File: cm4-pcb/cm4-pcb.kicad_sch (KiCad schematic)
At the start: 35 parts, among them J1 Conn_01x02_Pin, J2 Conn_01x02_Pin, J3 USB1125-GF-B, J4 Conn_02x03_Odd_Even, J5 Conn_01x04, J6 J0011D21NL, J7 Conn_01x02, J8 Conn_01x02, U1 Pfostenstecker_6_2x3, U2 Pfostenstecker_6_2x3, U5 SMD-PUSH-BTN

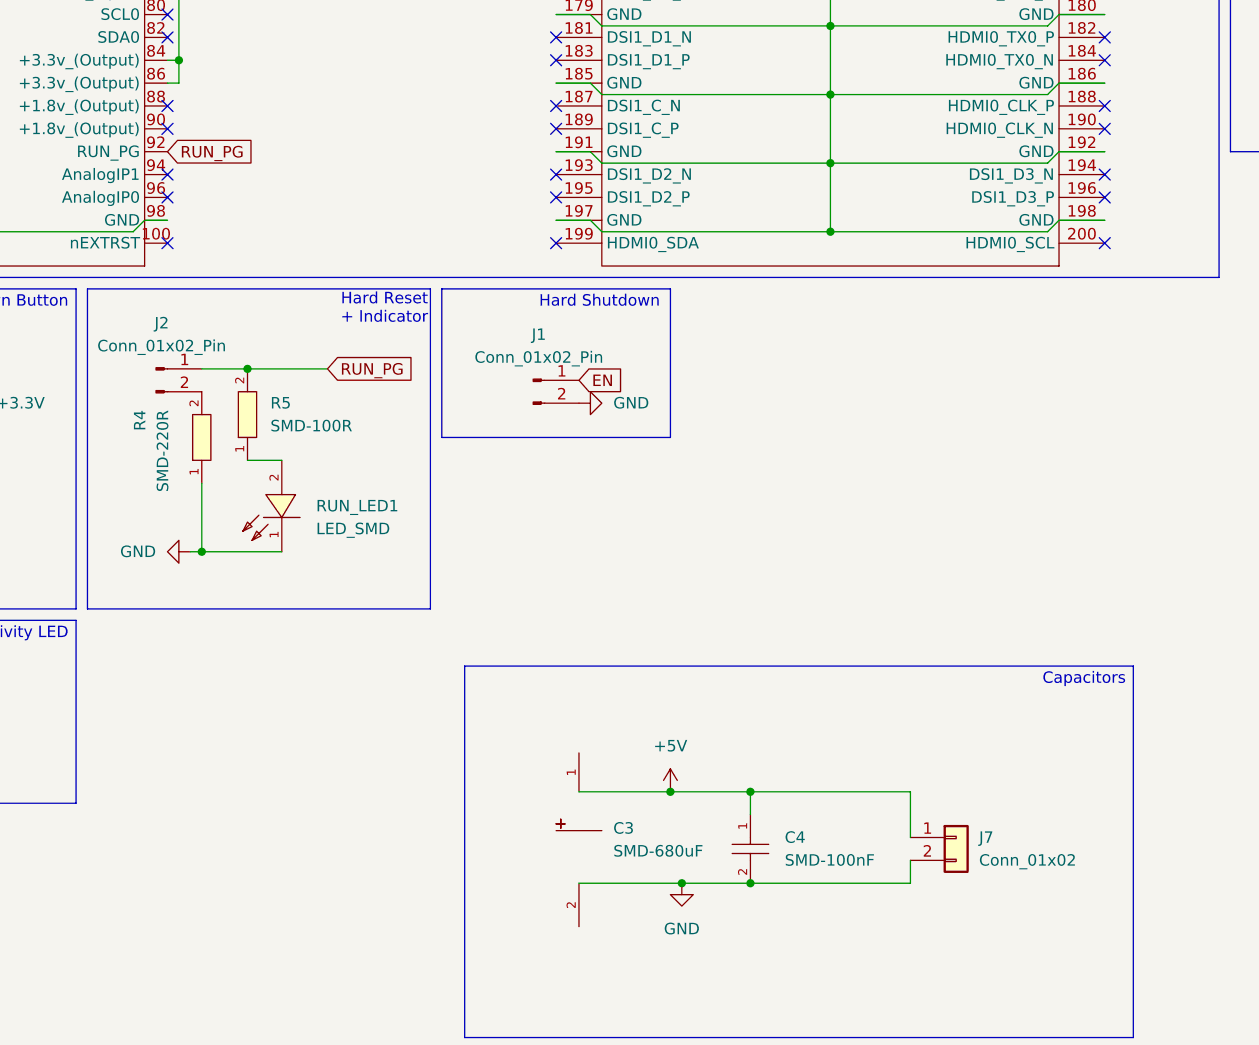
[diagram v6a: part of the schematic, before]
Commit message: Pins Analog Input
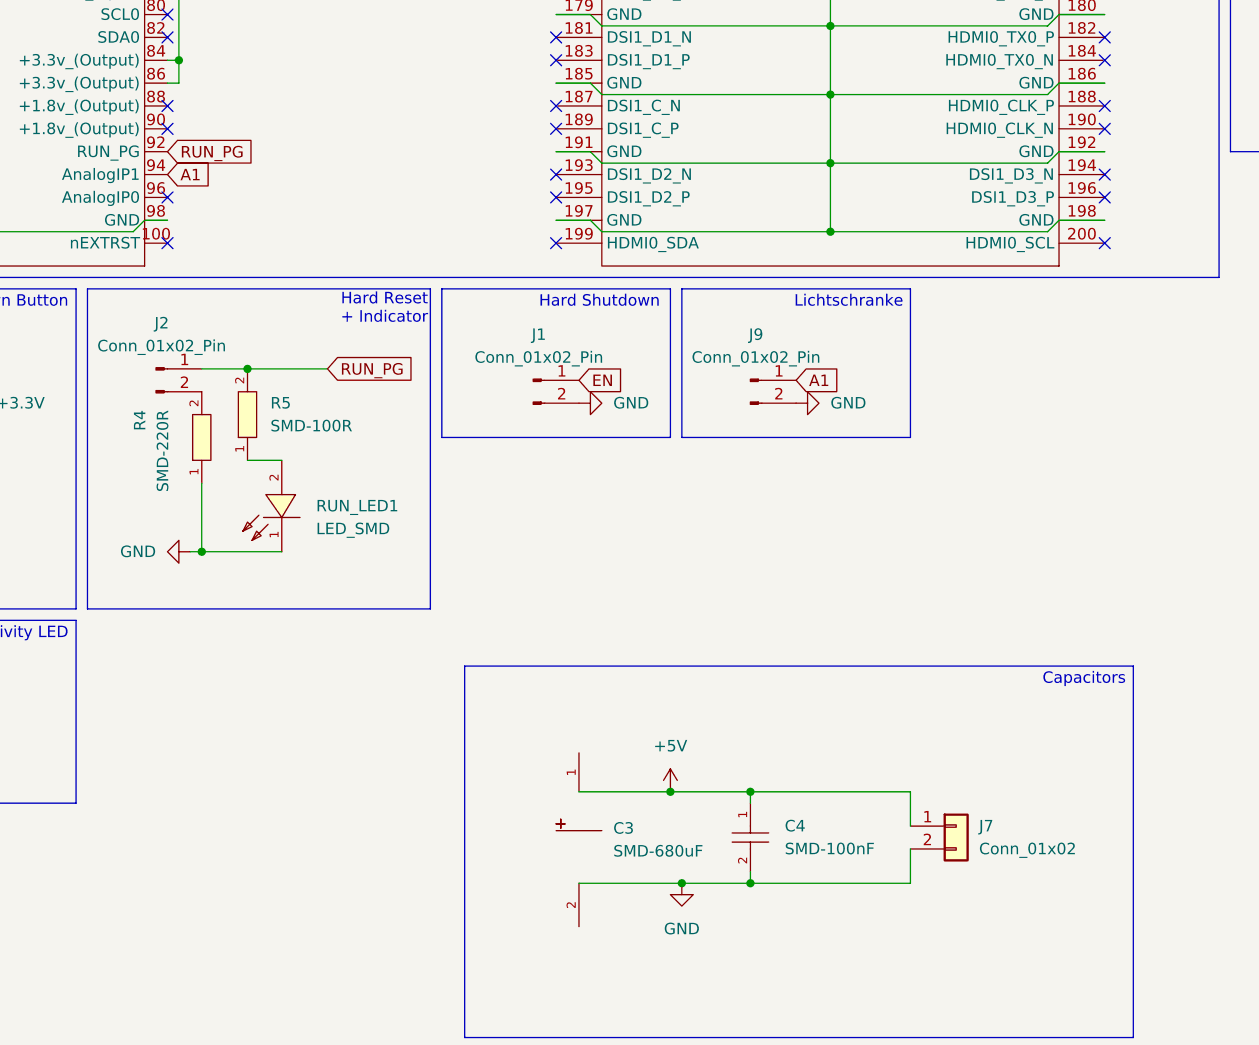
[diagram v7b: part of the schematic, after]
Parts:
- added J9: Conn_01x02_Pin, Connector_PinHeader_2.54mm:PinHeader_1x02_P2.54mm_Vertical, symbol Connector:Conn_01x02_Pin
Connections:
- net GND: now also J9.2 (Pin_2)
- net A1: now reaches Module1.94 (AnalogIP1)
- net A1: now also J9.1 (Pin_1)
- no-connect marks 126 -> 125
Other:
- note added: "Lichtschranke"
- moved on the sheet: C4, J7
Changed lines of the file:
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@@
 	)
 	(no_connect
-		(at 86.36 144.78)
-	)
-	(no_connect
 		(at 86.36 127)
 	)
@@
 	(wire
 		(pts
-			(xy 168.91 213.36) (xy 168.91 218.44)
+			(xy 168.91 213.36) (xy 168.91 217.17)
 		)
 		(stroke
@@
 	(wire
 		(pts
-			(xy 151.13 213.36) (xy 151.13 215.9)
+			(xy 151.13 213.36) (xy 151.13 214.63)
 		)
 		(stroke
@@
 	(wire
 		(pts
+			(xy 151.13 222.25) (xy 151.13 223.52)
+		)
+		(stroke
+			(width 0)
+			(type default)
+		)
+	)
+	(wire
+		(pts
 			(xy 55.88 95.25) (xy 55.88 102.87)
 		)
@@
 	(wire
 		(pts
-			(xy 168.91 220.98) (xy 168.91 223.52)
+			(xy 168.91 219.71) (xy 168.91 223.52)
 		)
 		(stroke
@@
 		)
 	)
+	(rectangle
+		(start 143.51 157.48)
+		(end 168.91 173.99)
+		(stroke
+			(width 0)
+			(type default)
+		)
+		(fill
+			(type none)
+		)
+	)
 	(text "Ethernet Magjack"
 		(exclude_from_sim no)
@@
 		)
 	)
+	(text "Lichtschranke"
+		(exclude_from_sim no)
+		(at 162.052 159.004 0)
+		(effects
+			(font
+				(size 1.27 1.27)
+			)
+		)
+	)
 	(text "Grounded for fixed use as USB Host, datasheet chapter 2.4 and pinout"
 		(exclude_from_sim no)
@@
 		)
 	)
+	(global_label "A1"
+		(shape input)
+		(at 156.21 167.64 0)
+		(fields_autoplaced yes)
+		(effects
+			(font
+				(size 1.27 1.27)
+			)
+			(justify left)
+		)
+		(property "Intersheetrefs" "${INTERSHEET_REFS}"
+			(at 161.4933 167.64 0)
+			(effects
+				(font
+					(size 1.27 1.27)
+				)
+				(justify left)
+				(hide yes)
+			)
+		)
+	)
 	(global_label "SDA"
 		(shape bidirectional)
@@
 		)
 	)
+	(global_label "A1"
+		(shape input)
+		(at 86.36 144.78 0)
+		(fields_autoplaced yes)
+		(effects
+			(font
+				(size 1.27 1.27)
+			)
+			(justify left)
+		)
+		(property "Intersheetrefs" "${INTERSHEET_REFS}"
+			(at 91.6433 144.78 0)
+			(effects
+				(font
+					(size 1.27 1.27)
+				)
+				(justify left)
+				(hide yes)
+			)
+		)
+	)
 	(global_label "SDA"
 		(shape bidirectional)
@@
 	)
 	(symbol
+		(lib_id "Connector:Conn_01x02_Pin")
+		(at 151.13 167.64 0)
+		(unit 1)
+		(exclude_from_sim no)
+		(in_bom yes)
+		(on_board yes)
+		(dnp no)
+		(fields_autoplaced yes)
+		(property "Reference" "J9"
+			(at 151.765 162.56 0)
+			(effects
+				(font
+					(size 1.27 1.27)
+				)
+			)
+		)
+		(property "Value" "Conn_01x02_Pin"
+			(at 151.765 165.1 0)
+			(effects
+				(font
+					(size 1.27 1.27)
+				)
+			)
+		)
+		(property "Footprint" "Connector_PinHeader_2.54mm:PinHeader_1x02_P2.54mm_Vertical"
+			(at 151.13 167.64 0)
+			(effects
+				(font
+					(size 1.27 1.27)
+				)
+				(hide yes)
+			)
+		)
+		(property "Datasheet" "~"
+			(at 151.13 167.64 0)
+			(effects
+				(font
+					(size 1.27 1.27)
+				)
+				(hide yes)
+			)
+		)
+		(property "Description" "Generic connector, single row, 01x02, script generated"
+			(at 151.13 167.64 0)
+			(effects
+				(font
+					(size 1.27 1.27)
+				)
+				(hide yes)
+			)
+		)
+		(pin "2"
+		)
+		(pin "1"
+		)
+		(instances
+			(project "cm4-pcb"
+				(path "/498e70b5-f2fd-4a95-9aba-8c3678ffa14c"
+					(reference "J9")
+					(unit 1)
+				)
+			)
+		)
+	)
+	(symbol
 		(lib_id "bohlebots.lib:+5V")
 		(at 364.49 40.64 90)
@@
 	(symbol
 		(lib_id "bohlebots.lib:SMD-100nF")
-		(at 151.13 219.71 270)
+		(at 151.13 218.44 270)
 		(unit 1)
 		(exclude_from_sim no)
@@
 		(fields_autoplaced yes)
 		(property "Reference" "C4"
-			(at 154.94 218.4399 90)
+			(at 154.94 217.1699 90)
 			(effects
 				(font
@@
 		)
 		(property "Value" "SMD-100nF"
-			(at 154.94 220.9799 90)
+			(at 154.94 219.7099 90)
 			(effects
 				(font
@@
 		)
 		(property "Footprint" "BohleBots:C0603"
-			(at 140.97 219.71 0)
+			(at 140.97 218.44 0)
 			(effects
 				(font
@@
 		)
 		(property "Datasheet" "https://item.szlcsc.com/362304.html"
-			(at 153.67 215.9 0)
+			(at 153.67 214.63 0)
 			(effects
 				(font
@@
 		)
 		(property "Description" ""
-			(at 151.13 219.71 0)
+			(at 151.13 218.44 0)
 			(effects
 				(font
@@
 		)
 		(property "LCSC" "C30926"
-			(at 151.13 219.71 0)
+			(at 151.13 218.44 0)
 			(effects
 				(font
@@
 	(symbol
 		(lib_id "Connector_Generic:Conn_01x02")
-		(at 173.99 218.44 0)
+		(at 173.99 217.17 0)
 		(unit 1)
 		(exclude_from_sim no)
@@
 		(fields_autoplaced yes)
 		(property "Reference" "J7"
-			(at 176.53 218.4399 0)
+			(at 176.53 217.1699 0)
 			(effects
 				(font
@@
 		)
 		(property "Value" "Conn_01x02"
-			(at 176.53 220.9799 0)
+			(at 176.53 219.7099 0)
 			(effects
 				(font
@@
 		)
 		(property "Footprint" "Connector_PinHeader_2.54mm:PinHeader_1x02_P2.54mm_Vertical"
-			(at 173.99 218.44 0)
+			(at 173.99 217.17 0)
 			(effects
 				(font
@@
 		)
 		(property "Datasheet" "~"
-			(at 173.99 218.44 0)
+			(at 173.99 217.17 0)
 			(effects
 				(font
@@
 		)
 		(property "Description" "Generic connector, single row, 01x02, script generated (kicad-library-utils/schlib/autogen/connector/)"
-			(at 173.99 218.44 0)
+			(at 173.99 217.17 0)
 			(effects
 				(font
@@
 					(unit 1)
 				)
+			)
+		)
+	)
+	(symbol
+		(lib_id "bohlebots.lib:GND")
+		(at 156.21 170.18 90)
+		(unit 1)
+		(exclude_from_sim no)
+		(in_bom yes)
+		(on_board yes)
+		(dnp no)
+		(fields_autoplaced yes)
+		(property "Reference" "#PWR047"
+			(at 162.56 170.18 0)
+			(effects
+				(font
+					(size 1.27 1.27)
+				)
+				(hide yes)
+			)
+		)
+		(property "Value" "GND"
+			(at 160.02 170.1799 90)
+			(effects
+				(font
+					(size 1.27 1.27)
+				)
+				(justify right)
+			)
+		)
+		(property "Footprint" ""
+			(at 156.21 170.18 0)
+			(effects
+				(font
+					(size 1.27 1.27)
+				)
+				(hide yes)
+			)
+		)
+		(property "Datasheet" ""
+			(at 156.21 170.18 0)
+			(effects
+				(font
+					(size 1.27 1.27)
+				)
+				(hide yes)
+			)
+		)
+		(property "Description" "Power symbol creates a global label with name \"GND\" , ground"
+			(at 156.21 170.18 0)
+			(effects
+				(font
+					(size 1.27 1.27)
+				)
+				(hide yes)
+			)
+		)
+		(pin "1"
+		)
+		(instances
+			(project "cm4-pcb"
+				(path "/498e70b5-f2fd-4a95-9aba-8c3678ffa14c"
+					(reference "#PWR047")
+					(unit 1)
+				)

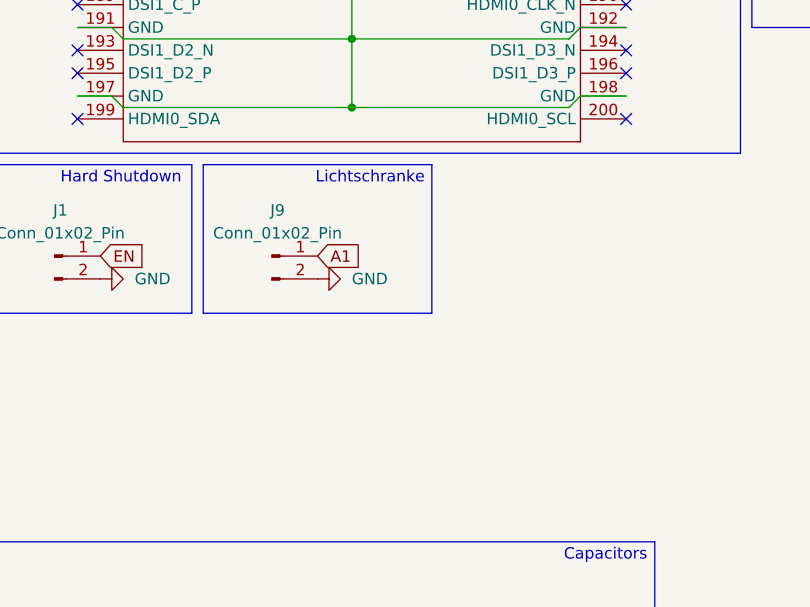
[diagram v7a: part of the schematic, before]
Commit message: Added AN Pullup resistor
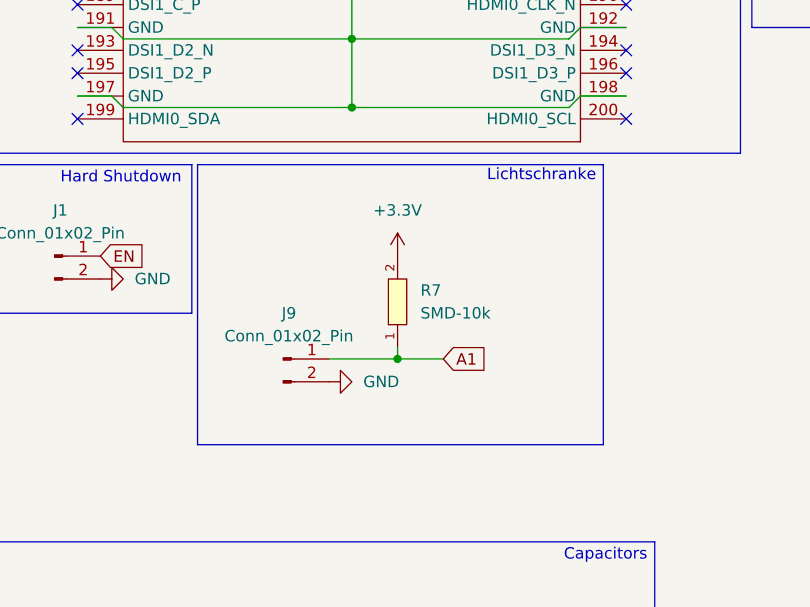
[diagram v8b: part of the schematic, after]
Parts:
- added R7: SMD-10k, BohleBots:R0603, symbol bohlebots.lib:SMD-10k
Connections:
- net +3.3V: now also R7.2
- net A1: now also R7.1
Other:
- moved on the sheet: J9
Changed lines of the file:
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@@
 	)
 	(junction
+		(at 165.1 179.07)
+		(diameter 0)
+		(color 0 0 0 0)
+	)
+	(junction
 		(at 142.24 213.36)
 		(diameter 0)
@@
 	(wire
 		(pts
+			(xy 165.1 177.8) (xy 165.1 179.07)
+		)
+		(stroke
+			(width 0)
+			(type default)
+		)
+	)
+	(wire
+		(pts
 			(xy 288.29 73.66) (xy 288.29 80.01)
 		)
@@
 	(wire
 		(pts
+			(xy 170.18 179.07) (xy 165.1 179.07)
+		)
+		(stroke
+			(width 0)
+			(type default)
+		)
+	)
+	(wire
+		(pts
 			(xy 133.35 58.42) (xy 134.62 59.69)
 		)
@@
 	(wire
 		(pts
+			(xy 165.1 179.07) (xy 157.48 179.07)
+		)
+		(stroke
+			(width 0)
+			(type default)
+		)
+	)
+	(wire
+		(pts
 			(xy 55.88 110.49) (xy 55.88 118.11)
 		)
@@
 	)
 	(rectangle
-		(start 143.51 157.48)
-		(end 168.91 173.99)
+		(start 142.875 157.48)
+		(end 187.96 188.595)
 		(stroke
 			(width 0)
@@
 	(text "Lichtschranke"
 		(exclude_from_sim no)
-		(at 162.052 159.004 0)
+		(at 181.102 158.75 0)
 		(effects
 			(font
@@
 	(global_label "A1"
 		(shape input)
-		(at 156.21 167.64 0)
+		(at 170.18 179.07 0)
 		(fields_autoplaced yes)
 		(effects
@@
 		)
 		(property "Intersheetrefs" "${INTERSHEET_REFS}"
-			(at 161.4933 167.64 0)
+			(at 175.4633 179.07 0)
 			(effects
 				(font
@@
 	(symbol
 		(lib_id "Connector:Conn_01x02_Pin")
-		(at 151.13 167.64 0)
+		(at 152.4 179.07 0)
 		(unit 1)
 		(exclude_from_sim no)
@@
 		(fields_autoplaced yes)
 		(property "Reference" "J9"
-			(at 151.765 162.56 0)
+			(at 153.035 173.99 0)
 			(effects
 				(font
@@
 		)
 		(property "Value" "Conn_01x02_Pin"
-			(at 151.765 165.1 0)
+			(at 153.035 176.53 0)
 			(effects
 				(font
@@
 		)
 		(property "Footprint" "Connector_PinHeader_2.54mm:PinHeader_1x02_P2.54mm_Vertical"
-			(at 151.13 167.64 0)
+			(at 152.4 179.07 0)
 			(effects
 				(font
@@
 		)
 		(property "Datasheet" "~"
-			(at 151.13 167.64 0)
+			(at 152.4 179.07 0)
 			(effects
 				(font
@@
 		)
 		(property "Description" "Generic connector, single row, 01x02, script generated"
-			(at 151.13 167.64 0)
+			(at 152.4 179.07 0)
 			(effects
 				(font
@@
 	)
 	(symbol
+		(lib_id "bohlebots.lib:SMD-10k")
+		(at 165.1 172.72 90)
+		(unit 1)
+		(exclude_from_sim no)
+		(in_bom yes)
+		(on_board yes)
+		(dnp no)
+		(fields_autoplaced yes)
+		(property "Reference" "R7"
+			(at 167.64 171.4499 90)
+			(effects
+				(font
+					(size 1.27 1.27)
+				)
+				(justify right)
+			)
+		)
+		(property "Value" "SMD-10k"
+			(at 167.64 173.9899 90)
+			(effects
+				(font
+					(size 1.27 1.27)
+				)
+				(justify right)
+			)
+		)
+		(property "Footprint" "BohleBots:R0603"
+			(at 175.26 172.72 0)
+			(effects
+				(font
+					(size 1.27 1.27)
+					(italic yes)
+				)
+				(hide yes)
+			)
+		)
+		(property "Datasheet" "https://www.mouser.in/datasheet/2/447/PYu_RT_1_to_0_01_RoHS_L_11-1669912.pdf"
+			(at 169.418 182.118 0)
+			(effects
+				(font
+					(size 1.27 1.27)
+				)
+				(justify left)
+				(hide yes)
+			)
+		)
+		(property "Description" ""
+			(at 165.1 172.72 0)
+			(effects
+				(font
+					(size 1.27 1.27)
+				)
+				(hide yes)
+			)
+		)
+		(property "LCSC" "C25804"
+			(at 165.1 172.72 0)
+			(effects
+				(font
+					(size 1.27 1.27)
+				)
+				(hide yes)
+			)
+		)
+		(pin "1"
+		)
+		(pin "2"
+		)
+		(instances
+			(project "cm4-pcb"
+				(path "/498e70b5-f2fd-4a95-9aba-8c3678ffa14c"
+					(reference "R7")
+					(unit 1)
+				)
+			)
+		)
+	)
+	(symbol
 		(lib_id "bohlebots.lib:GND")
 		(at 55.88 29.21 180)
@@
 	(symbol
 		(lib_id "bohlebots.lib:GND")
-		(at 156.21 170.18 90)
+		(at 157.48 181.61 90)
 		(unit 1)
 		(exclude_from_sim no)
@@
 		(fields_autoplaced yes)
 		(property "Reference" "#PWR047"
-			(at 162.56 170.18 0)
+			(at 163.83 181.61 0)
 			(effects
 				(font
@@
 		)
 		(property "Value" "GND"
-			(at 160.02 170.1799 90)
+			(at 161.29 181.6099 90)
 			(effects
 				(font
@@
 		)
 		(property "Footprint" ""
-			(at 156.21 170.18 0)
+			(at 157.48 181.61 0)
 			(effects
 				(font
@@
 		)
 		(property "Datasheet" ""
-			(at 156.21 170.18 0)
+			(at 157.48 181.61 0)
 			(effects
 				(font
@@
 		)
 		(property "Description" "Power symbol creates a global label with name \"GND\" , ground"
-			(at 156.21 170.18 0)
+			(at 157.48 181.61 0)
 			(effects
 				(font
@@
 					(unit 1)
 				)
+			)
+		)
+	)
+	(symbol
+		(lib_id "bohlebots.lib:+3.3V")
+		(at 165.1 167.64 0)
+		(unit 1)
+		(exclude_from_sim no)
+		(in_bom yes)
+		(on_board yes)
+		(dnp no)
+		(fields_autoplaced yes)
+		(property "Reference" "#PWR048"
+			(at 165.1 171.45 0)
+			(effects
+				(font
+					(size 1.27 1.27)
+				)
+				(hide yes)
+			)
+		)
+		(property "Value" "+3.3V"
+			(at 165.1 162.56 0)
+			(effects
+				(font
+					(size 1.27 1.27)
+				)
+			)
+		)
+		(property "Footprint" ""
+			(at 165.1 167.64 0)
+			(effects
+				(font
+					(size 1.27 1.27)
+				)
+				(hide yes)
+			)
+		)
+		(property "Datasheet" ""
+			(at 165.1 167.64 0)
+			(effects
+				(font
+					(size 1.27 1.27)
+				)
+				(hide yes)
+			)
+		)
+		(property "Description" "Power symbol creates a global label with name \"+3.3V\""
+			(at 165.1 167.64 0)
+			(effects
+				(font
+					(size 1.27 1.27)
+				)
+				(hide yes)
+			)
+		)
+		(pin "1"
+		)
+		(instances
+			(project "cm4-pcb"
+				(path "/498e70b5-f2fd-4a95-9aba-8c3678ffa14c"
+					(reference "#PWR048")
+					(unit 1)
+				)
